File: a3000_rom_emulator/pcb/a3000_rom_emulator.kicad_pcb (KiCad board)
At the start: 4 copper layers, 43.2 x 78.7 mm, 96 parts

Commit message: Arcflash-A v2 final; from a couple of weeks ago
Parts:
- added A21: rom_A19, Connector_PinHeader_2.54mm:PinHeader_1x01_P2.54mm_Vertical, F.Cu at (180.3, 41.9)
- added AEXTGND: Ground, Connector_PinHeader_2.54mm:PinHeader_1x01_P2.54mm_Vertical, F.Cu at (161.4, 38.8)
- moved RESET 4.32 mm to (166.8, 72.2), turned to 0 degrees
- moved R7 2.99 mm to (166.3, 90.6), turned to 180 degrees
- moved staple_single13 1.54 mm to (177.6, 34.3)
- moved staple_single11 0.75 mm to (176.0, 32.5)
- moved staple_single16 0.54 mm to (159.6, 33.8)
- moved R3 0.09 mm to (168.6, 77.6)
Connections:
- BUF pad 10: ndrive_arc_RESET -> GND
- BUF pad 11: arc_POR_R -> arc_RESET
- BUF pad 13: ndrive_arc_POR -> ndrive_arc_RESET
- BUF pad 4: GND -> ndrive_arc_POR
- BUF pad 5: arc_RESET -> GND
- BUF pad 6: arc_RESET_buffered -> arc_POR_R
- BUF pad 8: arc_RESET -> arc_RESET_buffered
- BUF pad 9: GND -> arc_RESET
- MCU pad 17: ndrive_arc_RESET -> arc_RESET_buffered
- MCU pad 18: ndrive_arc_POR -> ndrive_arc_RESET
- MCU pad 3: arc_RESET_buffered -> ndrive_arc_POR
- R6 pad 1: ndrive_arc_POR -> ndrive_arc_RESET
- R7 pad 1: ndrive_arc_RESET -> ndrive_arc_POR
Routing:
- net ndrive_arc_POR: track 25.6 -> 17.2 mm
- net arc_POR_R: track 2.71 -> 9.17 mm
- net arc_RESET_buffered: track 17.7 -> 24.1 mm
- net GND: track 88.3 -> 92.3 mm, vias 32 -> 31
- net rom_A19: track 69.6 -> 72.8 mm, vias 0 -> 1
- net arc_RESET: track 11.5 -> 10.1 mm
- net ndrive_arc_RESET: track 24.6 -> 25.9 mm
- net rom_A19_ext: track 28.2 -> 29.5 mm
- net rom_A16_ext: track 33.3 -> 34.4 mm
- net rom_A16: track 74.1 -> 75.0 mm
- net rom_A17: track 71.4 -> 70.6 mm
- net rom_nOE: track 15.7 -> 16.4 mm
- net rom_D7: track 27.9 -> 27.3 mm
- net rom_D31: track 42.7 -> 42.2 mm
- net rom_nOE_ext: track 7.37 -> 7.88 mm
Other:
- board text added: "Arcflash-A v2 2019-05-15 Phillip Pearson 2018 http://myelin.nz/arcflash"
- board text added: "GND OE A21 A20 A19 A18"
- board text added: "N W+E S"
- board text added: "eOE e21 e20 e19 e18"
- board text removed: "-- -- -- -- --"
- board text removed: "OE A21 A20 A19 A18"
- board text removed: "arcflash v2 2019-??-?? Phillip Pearson 2018 http://myelin.nz/arcflash"

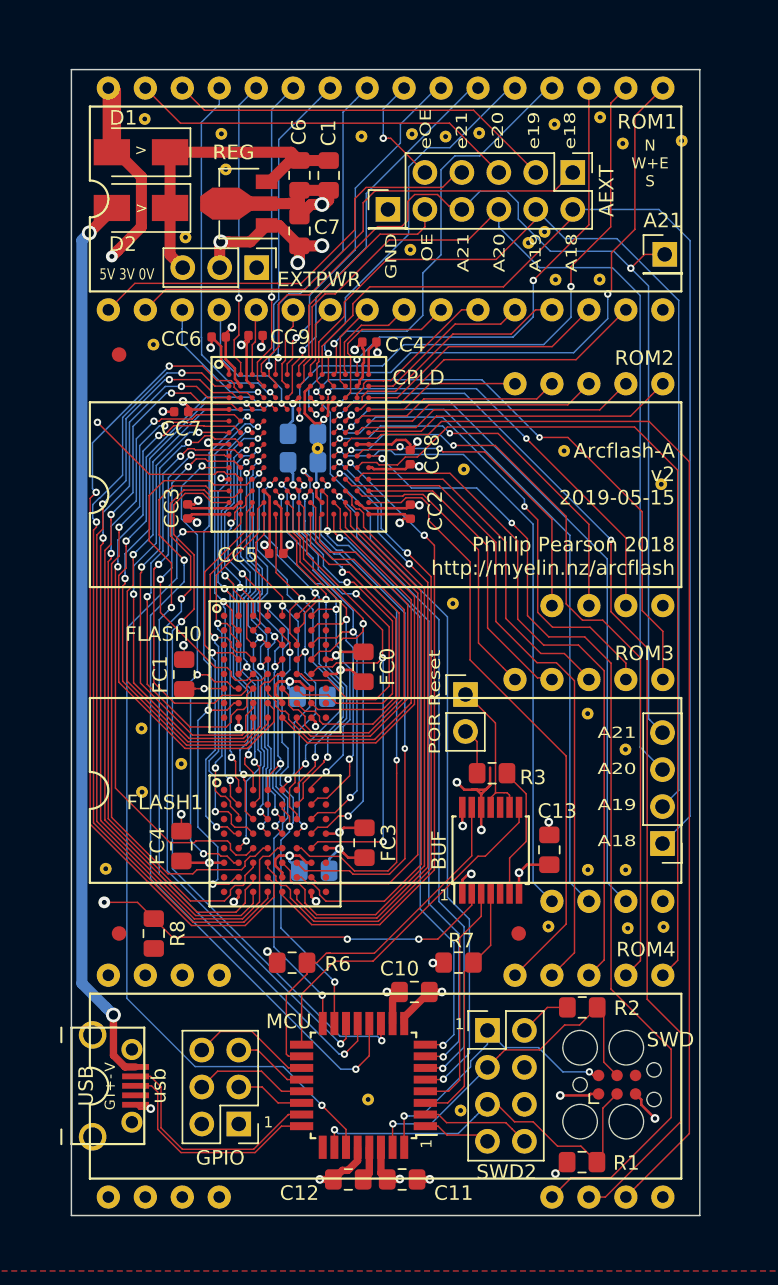
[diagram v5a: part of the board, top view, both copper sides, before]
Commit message: arcflash: v3 PCB with 68R resistor packs to provide some protection/damping to data lines
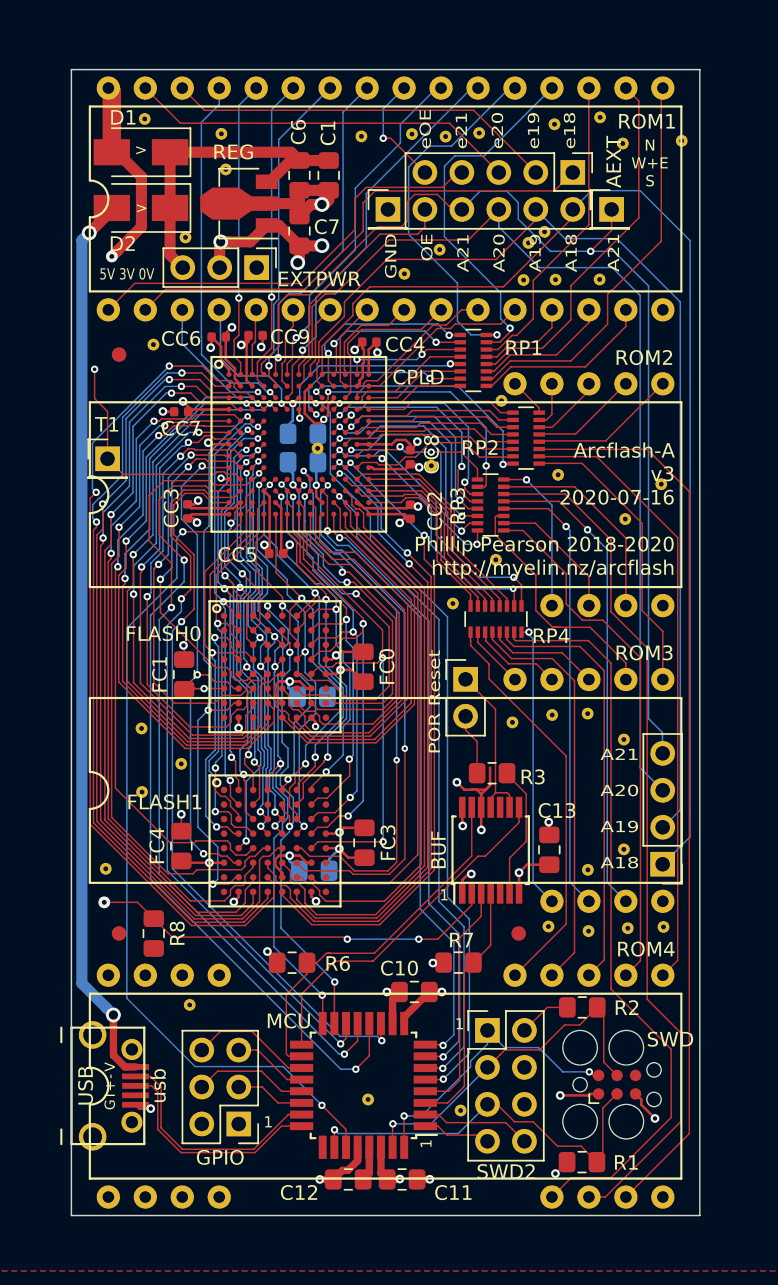
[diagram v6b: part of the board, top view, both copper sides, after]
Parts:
- added RP1: Pack of 8 x isolated 68R resistors, Resistor_SMD:R_Array_Convex_8x0602, F.Cu at (167.3, 49.2)
- added RP2: Pack of 8 x isolated 68R resistors, Resistor_SMD:R_Array_Convex_8x0602, F.Cu at (170.9, 54.5)
- added RP3: Pack of 8 x isolated 68R resistors, Resistor_SMD:R_Array_Convex_8x0602, F.Cu at (168.5, 59.1)
- added RP4: Pack of 8 x isolated 68R resistors, Resistor_SMD:R_Array_Convex_8x0602, F.Cu at (168.9, 67.0)
- added T1: rom_5V, Connector_PinHeader_2.54mm:PinHeader_1x01_P2.54mm_Vertical, F.Cu at (142.2, 56.0)
- added staple_single37: , myelin-kicad:via_single, F.Cu at (175.2, 88.4)
- added staple_single38: , myelin-kicad:via_single, F.Cu at (170.0, 74.1)
- added staple_single39: , myelin-kicad:via_single, F.Cu at (172.7, 73.6)
- added staple_single40: , myelin-kicad:via_single, F.Cu at (162.6, 43.2)
- added staple_single41: , myelin-kicad:via_single, F.Cu at (170.8, 43.7)
- added staple_single42: , myelin-kicad:via_single, F.Cu at (147.8, 93.5)
- added staple_single43: , myelin-kicad:via_single, F.Cu at (168.9, 62.9)
- added staple_single44: , myelin-kicad:via_single, F.Cu at (169.3, 52.0)
- added staple_single45: , myelin-kicad:via_single, F.Cu at (173.1, 57.1)
- BUF: value 74LVT125PW -> 74LVC125PW
- D2: value S1ATR -> S1ATR NF
- MCU: value ATSAMD21E18A -> ATSAMD21E18A-AU
- R6, R7: value NF 10k -> 10k
- moved staple_single28 6.29 mm to (177.8, 60.1)
- moved A21 4.78 mm to (176.7, 38.8)
- moved staple_single36 2.24 mm to (164.4, 56.4)
- moved staple_single19 2.01 mm to (165.0, 41.6)
- moved AEXT2 1.42 mm to (180.3, 83.8)
- moved staple_single4 1.42 mm to (177.7, 82.8)
- moved RESET 1.04 mm to (166.8, 71.1)
- moved staple_single5 0.69 mm to (177.7, 75.2)
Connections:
- ROM1 pad 13: rom_D0 -> rom_D0_ext
- ROM1 pad 14: rom_D1 -> rom_D1_ext
- ROM1 pad 15: rom_D2 -> rom_D2_ext
- ROM1 pad 17: rom_D3 -> rom_D3_ext
- ROM1 pad 18: rom_D4 -> rom_D4_ext
- ROM1 pad 19: rom_D5 -> rom_D5_ext
- ROM1 pad 20: rom_D6 -> rom_D6_ext
- ROM1 pad 21: rom_D7 -> rom_D7_ext
- ROM2 pad 13: rom_D8 -> rom_D8_ext
- ROM2 pad 14: rom_D9 -> rom_D9_ext
- ROM2 pad 15: rom_D10 -> rom_D10_ext
- ROM2 pad 17: rom_D11 -> rom_D11_ext
- ROM2 pad 18: rom_D12 -> rom_D12_ext
- ROM2 pad 19: rom_D13 -> rom_D13_ext
- ROM2 pad 20: rom_D14 -> rom_D14_ext
- ROM2 pad 21: rom_D15 -> rom_D15_ext
- ROM3 pad 13: rom_D16 -> rom_D16_ext
- ROM3 pad 14: rom_D17 -> rom_D17_ext
- ROM3 pad 15: rom_D18 -> rom_D18_ext
- ROM3 pad 17: rom_D19 -> rom_D19_ext
- ROM3 pad 18: rom_D20 -> rom_D20_ext
- ROM3 pad 19: rom_D21 -> rom_D21_ext
- ROM3 pad 20: rom_D22 -> rom_D22_ext
- ROM3 pad 21: rom_D23 -> rom_D23_ext
- ROM4 pad 13: rom_D24 -> rom_D24_ext
- ROM4 pad 14: rom_D25 -> rom_D25_ext
- ROM4 pad 15: rom_D26 -> rom_D26_ext
- ROM4 pad 17: rom_D27 -> rom_D27_ext
- ROM4 pad 18: rom_D28 -> rom_D28_ext
- ROM4 pad 19: rom_D29 -> rom_D29_ext
- ROM4 pad 20: rom_D30 -> rom_D30_ext
- ROM4 pad 21: rom_D31 -> rom_D31_ext
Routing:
- net rom_D26: track 77.8 -> 12.2 mm
- net rom_D26_ext: track 0.00 -> 61.8 mm
- net rom_D25_ext: track 0.00 -> 59.1 mm
- net rom_D25: track 74.1 -> 15.5 mm
- net rom_D24: track 69.0 -> 16.4 mm
- net rom_D24_ext: track 0.00 -> 51.2 mm
- net rom_D27: track 59.7 -> 12.0 mm
- net rom_D27_ext: track 0.00 -> 42.3 mm
- net rom_D28: track 53.0 -> 16.5 mm
- net rom_D28_ext: track 0.00 -> 36.5 mm
- net rom_D18_ext: track 0.00 -> 33.2 mm, vias 0 -> 1
- net rom_D18: track 47.9 -> 15.6 mm, vias 1 -> 2
- net rom_D29: track 47.3 -> 16.0 mm
- net rom_D17_ext: track 0.00 -> 31.2 mm, vias 0 -> 1
- net rom_D17: track 45.4 -> 14.5 mm, vias 1 -> 2
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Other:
- board text added: "Arcflash-A v3 2020-07-16 Phillip Pearson 2018-2020 http://myelin.nz/arcflash"
- board text removed: "Arcflash-A v2 2019-05-15 Phillip Pearson 2018 http://myelin.nz/arcflash"
